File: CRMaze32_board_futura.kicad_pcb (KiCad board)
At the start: 2 copper layers, 74 x 100 mm, 83 parts, among them J101 CONN_01X02, J102 CONN_01X02, J103 GYRO_ADXRS_2, P102 GYRO_ADXRS_1, P103 SERIAL, P104 ENC_1_IN, P105 ENC_1_POWER, P106 ENC_2_IN, P107 ENC_2_POWER, P108 MOTOR1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

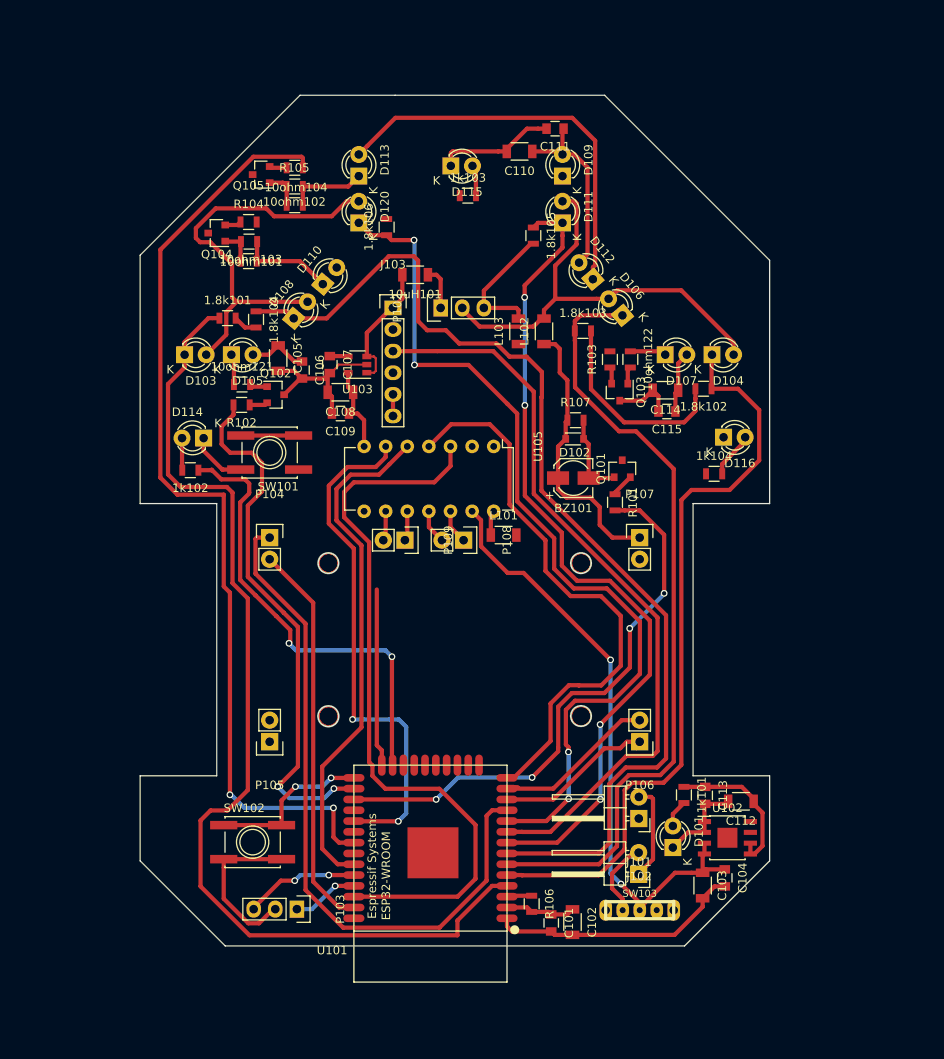
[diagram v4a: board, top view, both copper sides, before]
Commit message: arregladas referencias
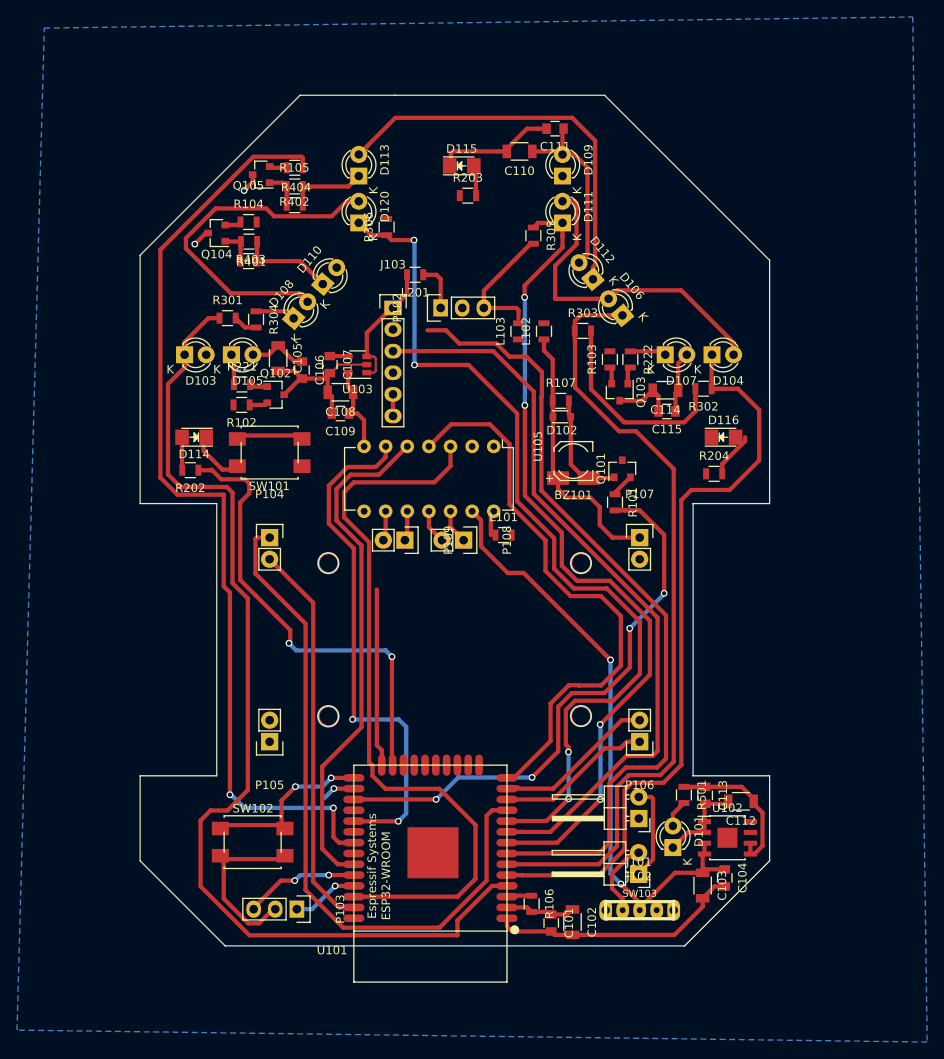
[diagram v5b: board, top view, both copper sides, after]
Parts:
- removed 10uH101: INDUCTOR, Capacitors_SMD:C_1206
- added L201: 10uH, Inductors_SMD:L_0805, F.Cu at (130.6, 51.6)
- D114, D115, D116: footprint LEDs:LED-3MM -> LEDs:LED_1206
- L101, L102, L103: footprint Capacitors_SMD:C_1206 -> Inductors_SMD:L_0805
- R202: renamed from 1k102; value R -> 1k
- R203: renamed from 1k103; value R -> 1k
- R204: renamed from 1k104; value R -> 1k
- R221: renamed from 10ohm121; value R -> 10ohm
- R222: renamed from 10ohm122; value R -> 10ohm
- R301: renamed from 1.8k101; value R -> 1.8k
- R302: renamed from 1.8k102; value R -> 1.8k
- R303: renamed from 1.8k103; value R -> 1.8k
- R304: renamed from 1.8k104; value R -> 1.8k
- R305: renamed from 1.8k105; value R -> 1.8k
- R306: renamed from 1.8k106; value R -> 1.8l
- R401: renamed from 10ohm101; value R -> 10ohm
- R402: renamed from 10ohm102; value R -> 10ohm
- R403: renamed from 10ohm103; value R -> 10ohm
- R404: renamed from 10ohm104; value R -> 10ohm
- R501: renamed from 1k101; value R -> 1k
- SW101, SW102: footprint Buttons_Switches_SMD:SW_SPST_EVQQ2 -> ESP32-footprints-Lib:smd_button
- moved D102 3.00 mm to (147.8, 68.3)
- moved R107 2.86 mm to (147.7, 66.4)
- moved D115 1.28 mm to (136.1, 38.8)
- moved D114 1.12 mm to (104.6, 70.7)
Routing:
- net GPIO_IR_FL: track 63.0 -> 3.95 mm, vias 2 -> 1
- net IN_IR4: track 125.7 -> 99.2 mm
- net VA3.3: track 101.8 -> 80.5 mm
- net GND: track 111.2 -> 115.6 mm, vias 0 -> 2
- net Net-(BZ101-Pad2): track 10.1 -> 13.4 mm
- net V3.3: track 51.3 -> 50.2 mm
- net A5V: track 5.11 -> 5.66 mm
- added copper zone on B.Cu, net GND

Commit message: enrutado OK
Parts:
- removed L101, L103: SPLITTER, Inductors_SMD:L_0805
- moved SW101 44.9 mm to (102.7, 116.1), turned to 270 degrees
- moved R301 5.07 mm to (103.5, 57.2), turned to 90 degrees
- moved D104 2.60 mm to (168.1, 61.1), turned to 180 degrees
- moved D107 2.50 mm to (162.5, 61.1), turned to 180 degrees
- moved C109 1.17 mm to (121.4, 69.0)
- moved SW102 1.12 mm to (112.6, 118.5), turned to 270 degrees
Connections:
- P102 pad 3: AGND -> GND
- R301 pad 2: AGND -> GND
- R302 pad 2: AGND -> GND
- R303 pad 2: AGND -> GND
- R304 pad 2: AGND -> GND
- R305 pad 2: AGND -> GND
- R306 pad 2: AGND -> GND
- U105 pad 14: MGND -> GND
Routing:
- net V3.3: track 50.2 -> 172.6 mm, vias 0 -> 5
- net 5V: track 69.4 -> 176.6 mm, vias 0 -> 3
- net GPIO_IR_DIAG: track 0.00 -> 80.3 mm, vias 0 -> 4
- net GPIO_IR_FR: track 0.00 -> 71.6 mm, vias 0 -> 4
- net GPIO_LED2: track 20.9 -> 86.5 mm, vias 0 -> 2
- net GPIO_IR_FL: track 3.95 -> 63.8 mm, vias 1 -> 2
- net GND: track 115.6 -> 175.0 mm, vias 2 -> 19
- net VA3.3: track 80.5 -> 136.3 mm
- net GPIO_LED3: track 0.00 -> 48.1 mm, vias 0 -> 2
- net Net-(R106-Pad1): track 9.75 -> 57.5 mm
- net AGND: track 42.1 -> 0.00 mm
- net Net-(D109-Pad1): track 0.00 -> 40.7 mm
- net IN_IR4: track 99.2 -> 118.1 mm, vias 0 -> 2
- net IN_IR1: track 122.4 -> 111.5 mm
- net Net-(SW102-Pad1): track 19.3 -> 12.1 mm
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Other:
- board size 74 x 100 mm -> 74 x 100.4 mm
- board text added: "+"
- board text added: "3.3"
- board text added: "A"
- board text added: "B"
- board text added: "CGS & VUU"
- board text added: "CRMaze32"
- board text added: "Club de Robótica y Mecatrónica"
- board text added: "EN"
- board text added: "GND"
- board text added: "IN"
- board text added: "IO_0"
- board text added: "RX"
- board text added: "TX"
- board text added: "UAM"

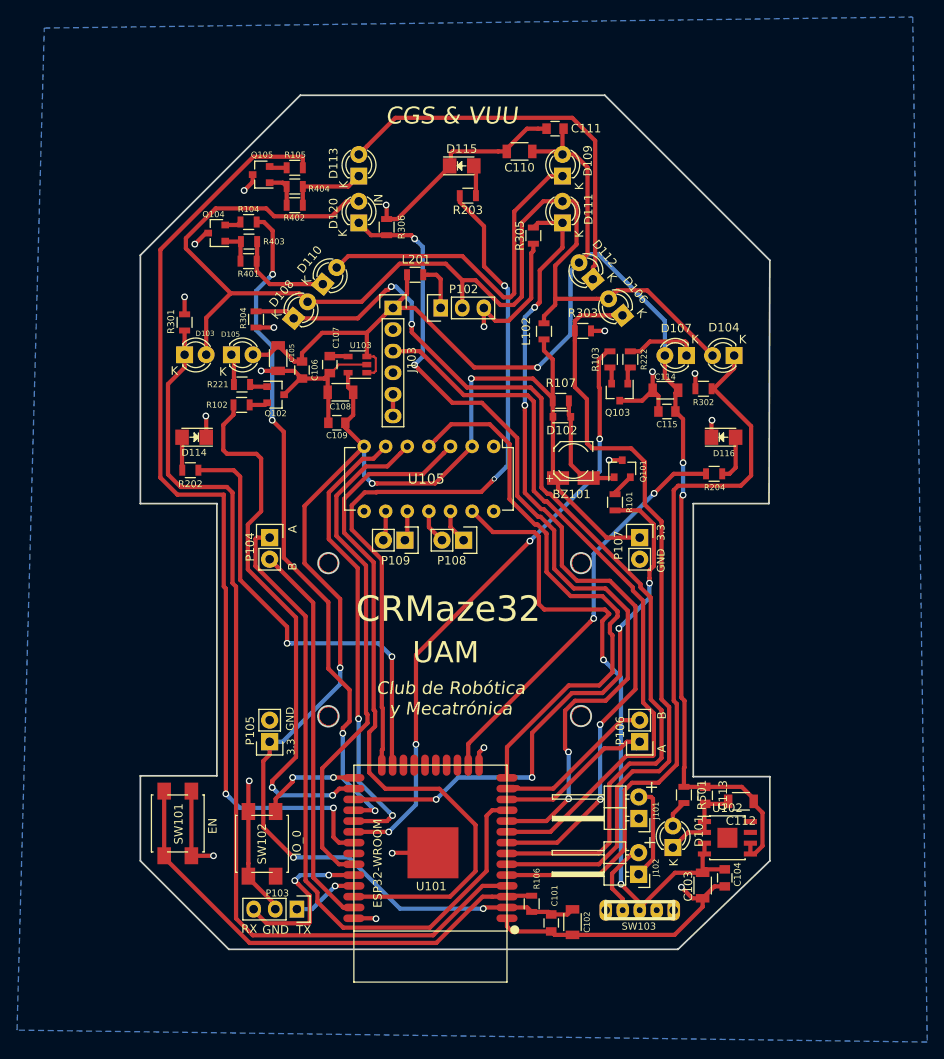
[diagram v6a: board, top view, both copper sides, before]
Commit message: enrutado finalizado y serigrafia OK
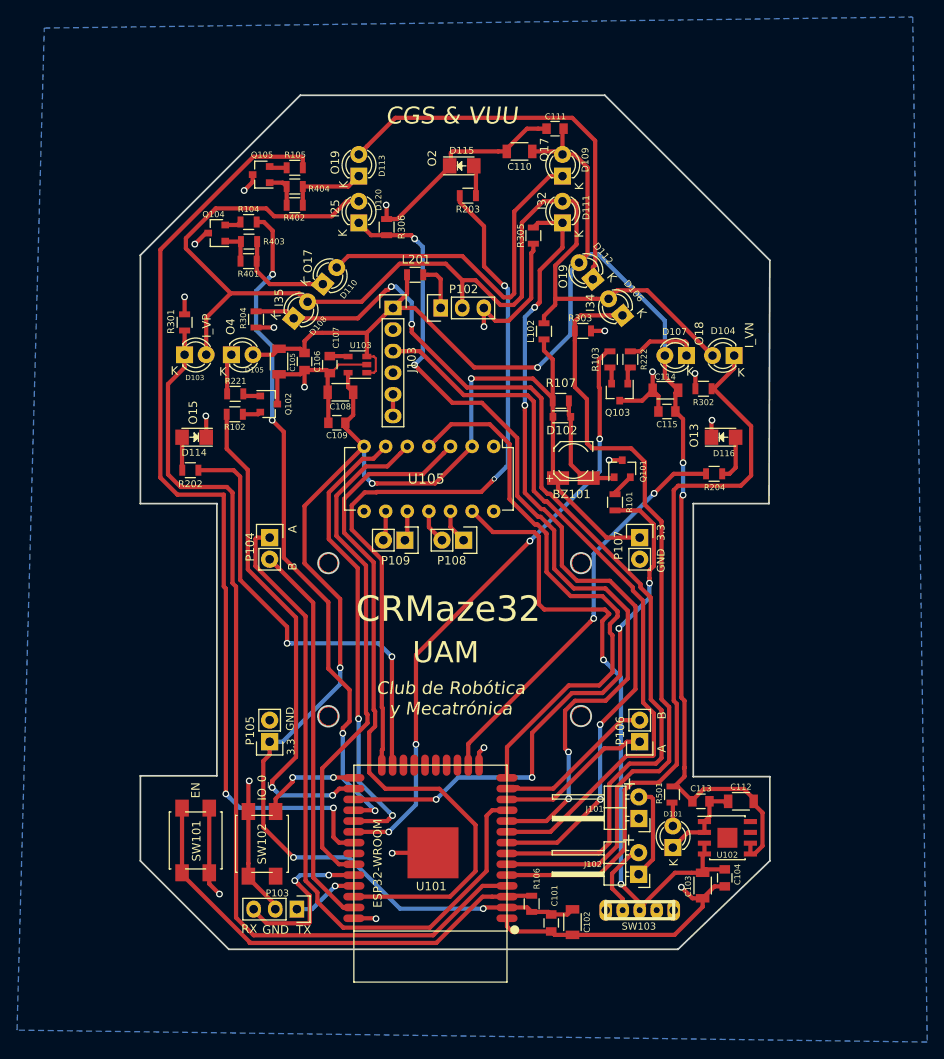
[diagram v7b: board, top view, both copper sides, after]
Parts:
- moved SW101 2.90 mm to (104.8, 118.1)
- moved R501 1.40 mm to (160.8, 112.7)
- moved Q102 1.36 mm to (113.4, 66.8)
- moved R102 1.36 mm to (109.4, 68.0)
- moved R221 1.36 mm to (109.5, 65.6)
- moved C106 1.04 mm to (117.6, 61.8)
- moved C113 0.86 mm to (164.2, 113.5), turned to 0 degrees
- moved C105 0.41 mm to (114.6, 61.8)
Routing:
- net GPIO_IR_FL: track 63.8 -> 58.7 mm
- net Net-(R106-Pad1): track 57.5 -> 54.6 mm
- net 5V: track 176.6 -> 179.3 mm
- net Net-(D105-Pad1): track 3.62 -> 5.23 mm
- net GND: track 175.0 -> 176.1 mm
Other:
- board text added: "I25"
- board text added: "I32"
- board text added: "I34"
- board text added: "I35"
- board text added: "I_VN"
- board text added: "I_VP"
- board text added: "O13"
- board text added: "O15"
- board text added: "O17"
- board text added: "O18"
- board text added: "O19"
- board text added: "O2"
- board text added: "O4"
- board text removed: "IN"
